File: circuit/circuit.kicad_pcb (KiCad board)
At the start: 2 copper layers, 3 parts, among them J1 USB_B_Mini, U1 ESP-WROOM-02, U2 nRF52820-QDAA

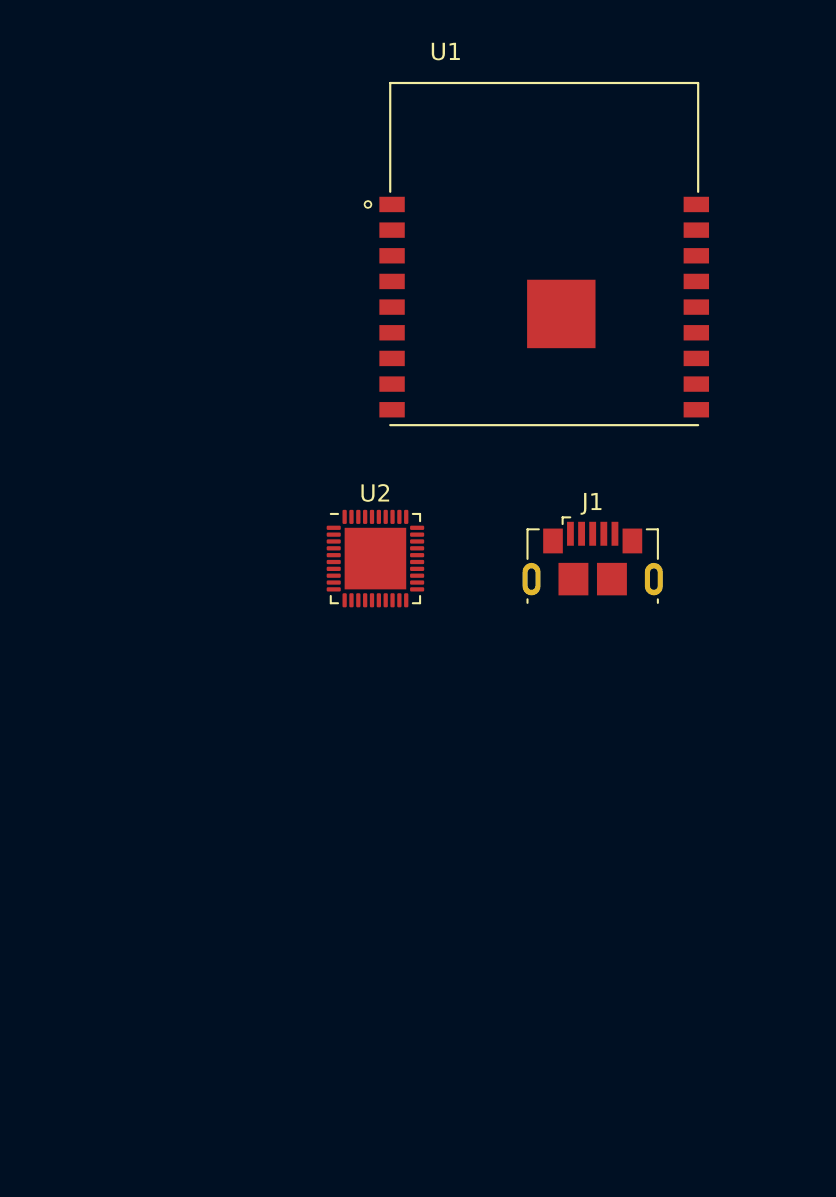
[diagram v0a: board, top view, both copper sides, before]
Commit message: change(mdbt50): use module for 802.15.4
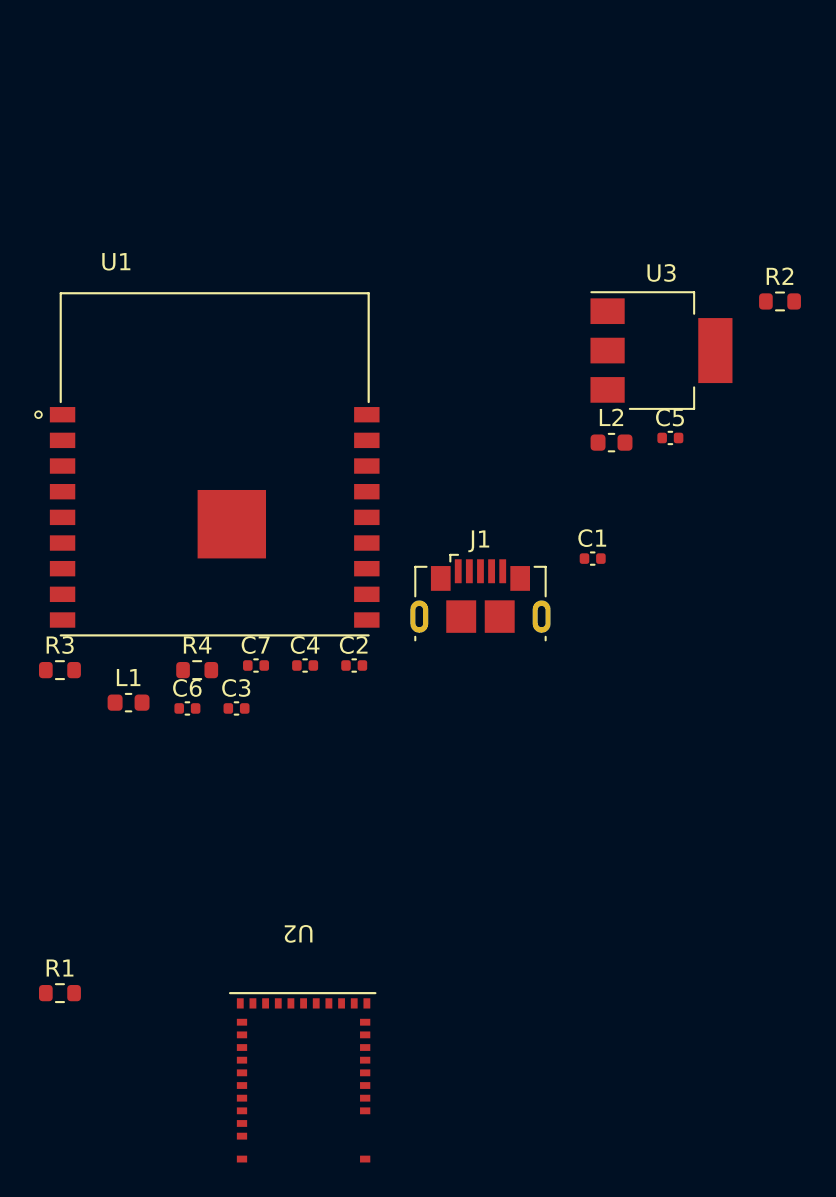
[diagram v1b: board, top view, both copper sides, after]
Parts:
- added C1: 22uF/10V 20%, Capacitor_SMD:C_0402_1005Metric, F.Cu at (152.4, 101.6)
- added C2: 22uF/10V 20%, Capacitor_SMD:C_0402_1005Metric, F.Cu at (138.5, 107.8)
- added C3: 10uF/25V, Capacitor_SMD:C_0402_1005Metric, F.Cu at (131.6, 110.4)
- added C4: 0.1uF/50V, Capacitor_SMD:C_0402_1005Metric, F.Cu at (135.6, 107.8)
- added C5: 1uF, Capacitor_SMD:C_0402_1005Metric, F.Cu at (156.9, 94.5)
- added C6: 10uF, Capacitor_SMD:C_0402_1005Metric, F.Cu at (128.7, 110.4)
- added C7: 10uF, Capacitor_SMD:C_0402_1005Metric, F.Cu at (132.7, 107.8)
- added L1: 10uH, Inductor_SMD:L_0603_1608Metric, F.Cu at (125.3, 110.0)
- added L2: 15nH, Inductor_SMD:L_0603_1608Metric, F.Cu at (153.5, 94.8)
- added R1: 0, Resistor_SMD:R_0603_1608Metric, F.Cu at (121.3, 127.0)
- added R2: 0, Resistor_SMD:R_0603_1608Metric, F.Cu at (163.3, 86.6)
- added R3: 0, Resistor_SMD:R_0603_1608Metric, F.Cu at (121.3, 108.1)
- added R4: 0, Resistor_SMD:R_0603_1608Metric, F.Cu at (129.3, 108.1)
- added U3: AMS1117-3.3, Package_TO_SOT_SMD:SOT-223-3_TabPin2, F.Cu at (156.4, 89.4)
- U1: value ESP-WROOM-02 -> ESP-C3-WROOM-02
- U2: value nRF52820-QDAA -> MDBT50; footprint Package_DFN_QFN:QFN-40-1EP_5x5mm_P0.4mm_EP3.6x3.6mm -> Module:MDBT50
- moved U2 25.4 mm to (139.7, 127.0), turned to 180 degrees
- moved U1 22.8 mm to (130.3, 98.1)
- moved J1 6.92 mm to (145.8, 103.8)
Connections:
- J1 pad 1: unconnected-(J1-Pad1) -> (no net)
- J1 pad 2: unconnected-(J1-Pad2) -> (no net)
- J1 pad 3: unconnected-(J1-Pad3) -> (no net)
- J1 pad 5: unconnected-(J1-Pad5) -> GND
- J1 pad 6: unconnected-(J1-Pad6) -> GND
- U1 pad 11: unconnected-(U1-Pad11) -> /ESP_UART_RX
- U1 pad 12: unconnected-(U1-Pad12) -> /ESP_UART_TX
- U1 pad 14: unconnected-(U1-Pad14) -> (no net)
- U1 pad 15: (no net) -> unconnected-(U1-Pad15)
- U1 pad 18: (no net) -> unconnected-(U1-Pad18)
- U1 pad 19: (no net) -> GND
- U1 pad 9: (no net) -> GND
- U2 pad 1: (no net) -> GND
- U2 pad 10: (no net) -> GND
- U2 pad 11: (no net) -> unconnected-(U2-Pad11)
- U2 pad 12: (no net) -> unconnected-(U2-Pad12)
- U2 pad 13: (no net) -> unconnected-(U2-Pad13)
- U2 pad 14: (no net) -> unconnected-(U2-Pad14)
- U2 pad 15: (no net) -> unconnected-(U2-Pad15)
- U2 pad 16: (no net) -> unconnected-(U2-Pad16)
- U2 pad 17: (no net) -> unconnected-(U2-Pad17)
- U2 pad 2: (no net) -> unconnected-(U2-Pad2)
- U2 pad 20: (no net) -> GND
- U2 pad 23: (no net) -> unconnected-(U2-Pad23)
- U2 pad 24: (no net) -> unconnected-(U2-Pad24)
- U2 pad 26: (no net) -> unconnected-(U2-Pad26)
- U2 pad 27: (no net) -> unconnected-(U2-Pad27)
- U2 pad 28: (no net) -> unconnected-(U2-Pad28)
- U2 pad 29: (no net) -> unconnected-(U2-Pad29)
- U2 pad 3: (no net) -> unconnected-(U2-Pad3)
- U2 pad 30: (no net) -> unconnected-(U2-Pad30)
- U2 pad 31: (no net) -> GND
- U2 pad 4: (no net) -> unconnected-(U2-Pad4)
- U2 pad 5: (no net) -> unconnected-(U2-Pad5)
- U2 pad 7: (no net) -> unconnected-(U2-Pad7)
- U2 pad 8: (no net) -> GND
